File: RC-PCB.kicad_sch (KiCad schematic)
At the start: 32 parts

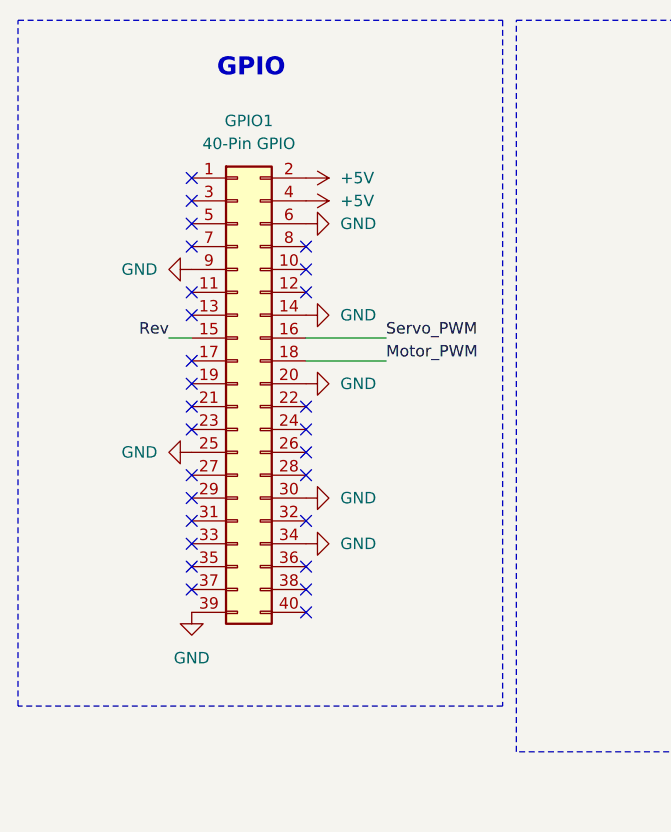
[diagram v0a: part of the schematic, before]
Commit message: fixed fins, moved stuff around
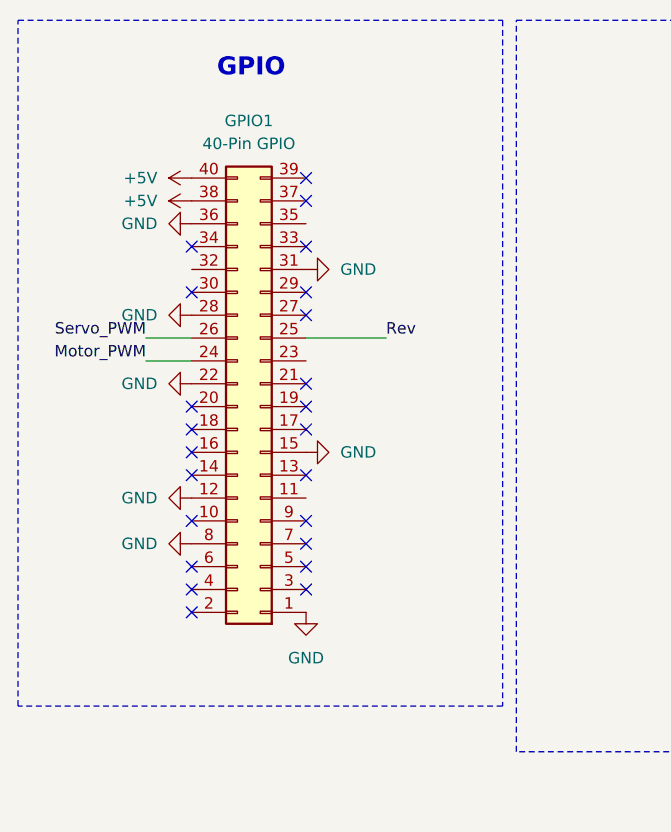
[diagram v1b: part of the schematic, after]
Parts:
- Battery1: footprint Connector_Molex:Molex_Micro-Fit_3.0_43650-0200_1x02_P3.00mm_Horizontal -> Connector_Molex:Molex_Micro-Fit_3.0_43650-0215_1x02_P3.00mm_Vertical
- Motor1: footprint Connector_Molex:Molex_Nano-Fit_105313-xx05_1x05_P2.50mm_Horizontal -> Connector_Molex:Molex_Nano-Fit_105309-xx05_1x05_P2.50mm_Vertical
- Servo1: footprint Connector_PinHeader_2.54mm:PinHeader_1x03_P2.54mm_Horizontal -> Connector_PinHeader_2.54mm:PinHeader_1x03_P2.54mm_Vertical
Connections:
- net +5V: now also GPIO1.38 (Pin_38), GPIO1.40 (Pin_40); no longer GPIO1.2 (Pin_2), GPIO1.4 (Pin_4)
- net GND: now also GPIO1.1 (Pin_1), GPIO1.12 (Pin_12), GPIO1.15 (Pin_15), GPIO1.22 (Pin_22), GPIO1.28 (Pin_28), GPIO1.31 (Pin_31), GPIO1.36 (Pin_36), GPIO1.8 (Pin_8); no longer GPIO1.14 (Pin_14), GPIO1.20 (Pin_20), GPIO1.25 (Pin_25), GPIO1.30 (Pin_30), GPIO1.34 (Pin_34), GPIO1.39 (Pin_39), GPIO1.6 (Pin_6), GPIO1.9 (Pin_9)
- net Motor_PWM: now also GPIO1.24 (Pin_24); no longer GPIO1.18 (Pin_18)
- net Rev: now also GPIO1.25 (Pin_25); no longer GPIO1.15 (Pin_15)
- net Servo_PWM: now also GPIO1.26 (Pin_26); no longer GPIO1.16 (Pin_16)
- no-connect marks 27 -> 23
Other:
- moved on the sheet: GPIO1

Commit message: finished routing
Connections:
- no-connect marks 23 -> 27
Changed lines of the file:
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@@
+	)
+	(no_connect
+		(at 50.8 76.2)
 	)
 	(no_connect
@@
 	)
 	(no_connect
+		(at 38.1 81.28)
+	)
+	(no_connect
 		(at 38.1 109.22)
 	)
@@
 	(no_connect
 		(at 38.1 99.06)
+	)
+	(no_connect
+		(at 50.8 91.44)
 	)
 	(no_connect
@@
 	)
 	(no_connect
+		(at 50.8 106.68)
+	)
+	(no_connect

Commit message: ready to order
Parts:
- +12V1, +5V1, GND1, Motor2, Power1, Rev2, Servo1, Servo2: now left out of the parts list
- 12VPWR1, 5VPWR1, REV1: footprint LED_SMD:LED_0805_2012Metric -> LED_SMD:LED_0805_2012Metric_Pad1.15x1.40mm_HandSolder; P/N (none) -> 150080VS75000
- Battery1: P/N (none) -> 436500215
- Cboot1, Cinx1: footprint Capacitor_SMD:C_0805_2012Metric -> Capacitor_SMD:C_0805_2012Metric_Pad1.18x1.45mm_HandSolder; P/N (none) -> C0805C104K5RAC7411
- Cff1: footprint Capacitor_SMD:C_0805_2012Metric -> Capacitor_SMD:C_0805_2012Metric_Pad1.18x1.45mm_HandSolder; P/N (none) -> 08053A470JAT2A
- Cin1: footprint Capacitor_SMD:C_0805_2012Metric -> Capacitor_SMD:C_0805_2012Metric_Pad1.18x1.45mm_HandSolder; P/N (none) -> EMK212ABJ106KG-T
- Cout1: footprint Capacitor_SMD:C_0805_2012Metric -> Capacitor_SMD:C_0805_2012Metric_Pad1.18x1.45mm_HandSolder; P/N (none) -> GMC04Y5V224Z16NT
- GPIO1: P/N (none) -> 2222
- L1: footprint Inductor_SMD:L_0805_2012Metric -> Inductor_SMD:L_1008_2520Metric_Pad1.43x2.20mm_HandSolder; P/N (none) -> CIGB252012AG3R3MPE
- Motor1: P/N (none) -> 1053091105
- R1: footprint Resistor_SMD:R_0805_2012Metric -> Resistor_SMD:R_0805_2012Metric_Pad1.20x1.40mm_HandSolder; now left out of the parts list
- R2: footprint Resistor_SMD:R_0805_2012Metric -> Resistor_SMD:R_0805_2012Metric_Pad1.20x1.40mm_HandSolder; P/N (none) -> RK73B2ATTE512J
- R3: footprint Resistor_SMD:R_0805_2012Metric -> Resistor_SMD:R_0805_2012Metric_Pad1.20x1.40mm_HandSolder; P/N (none) -> ERA-6AEB152V
- R4: value 650 -> 620; footprint Resistor_SMD:R_0805_2012Metric -> Resistor_SMD:R_0805_2012Metric_Pad1.20x1.40mm_HandSolder; P/N (none) -> ERA-6AEB621V
- Ren1: footprint Resistor_SMD:R_0805_2012Metric -> Resistor_SMD:R_0805_2012Metric_Pad1.20x1.40mm_HandSolder; P/N (none) -> ERJ-6ENF1003V
- Rfbb1: footprint Resistor_SMD:R_0805_2012Metric -> Resistor_SMD:R_0805_2012Metric_Pad1.20x1.40mm_HandSolder; P/N (none) -> ERA-6AEB303V
- Rfbt1: footprint Resistor_SMD:R_0805_2012Metric -> Resistor_SMD:R_0805_2012Metric_Pad1.20x1.40mm_HandSolder; P/N (none) -> ERJ-6ENF2203V
- U1: P/N (none) -> TPS562243DRLR
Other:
- note added: "Should work hopefully"
- note removed: "Needs to be checked by someone smart"
- moved on the sheet: +12V1, +5V1, 12VPWR1, 5VPWR1, Battery1, Cboot1, Cff1, Cin1, Cinx1, Cout1, GND1, GPIO1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

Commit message: ready to order pt 2
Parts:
- added C1, C3: .1uF, Capacitor_SMD:C_0805_2012Metric_Pad1.18x1.45mm_HandSolder, symbol Device:C_Small
- added C2, C4, C5, C6: 10uF, Capacitor_SMD:C_0805_2012Metric_Pad1.18x1.45mm_HandSolder, symbol Device:C_Small
- Cin1: P/N EMK212ABJ106KG-T -> CGA4J1X7S1C106M125AE
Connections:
- net +12V: now also C1.1, C2.1, C6.1
- net +5V: now also C3.1, C4.1, C5.1
- net GND: now also C1.2, C2.2, C3.2, C4.2, C5.2, C6.2
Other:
- moved on the sheet: R1
